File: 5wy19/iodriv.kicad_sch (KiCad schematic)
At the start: 5 parts, among them IC10 MC33385, IC3 74HCT574, IC4 HIP0045, IC6 MC33385, IC8 MC33385

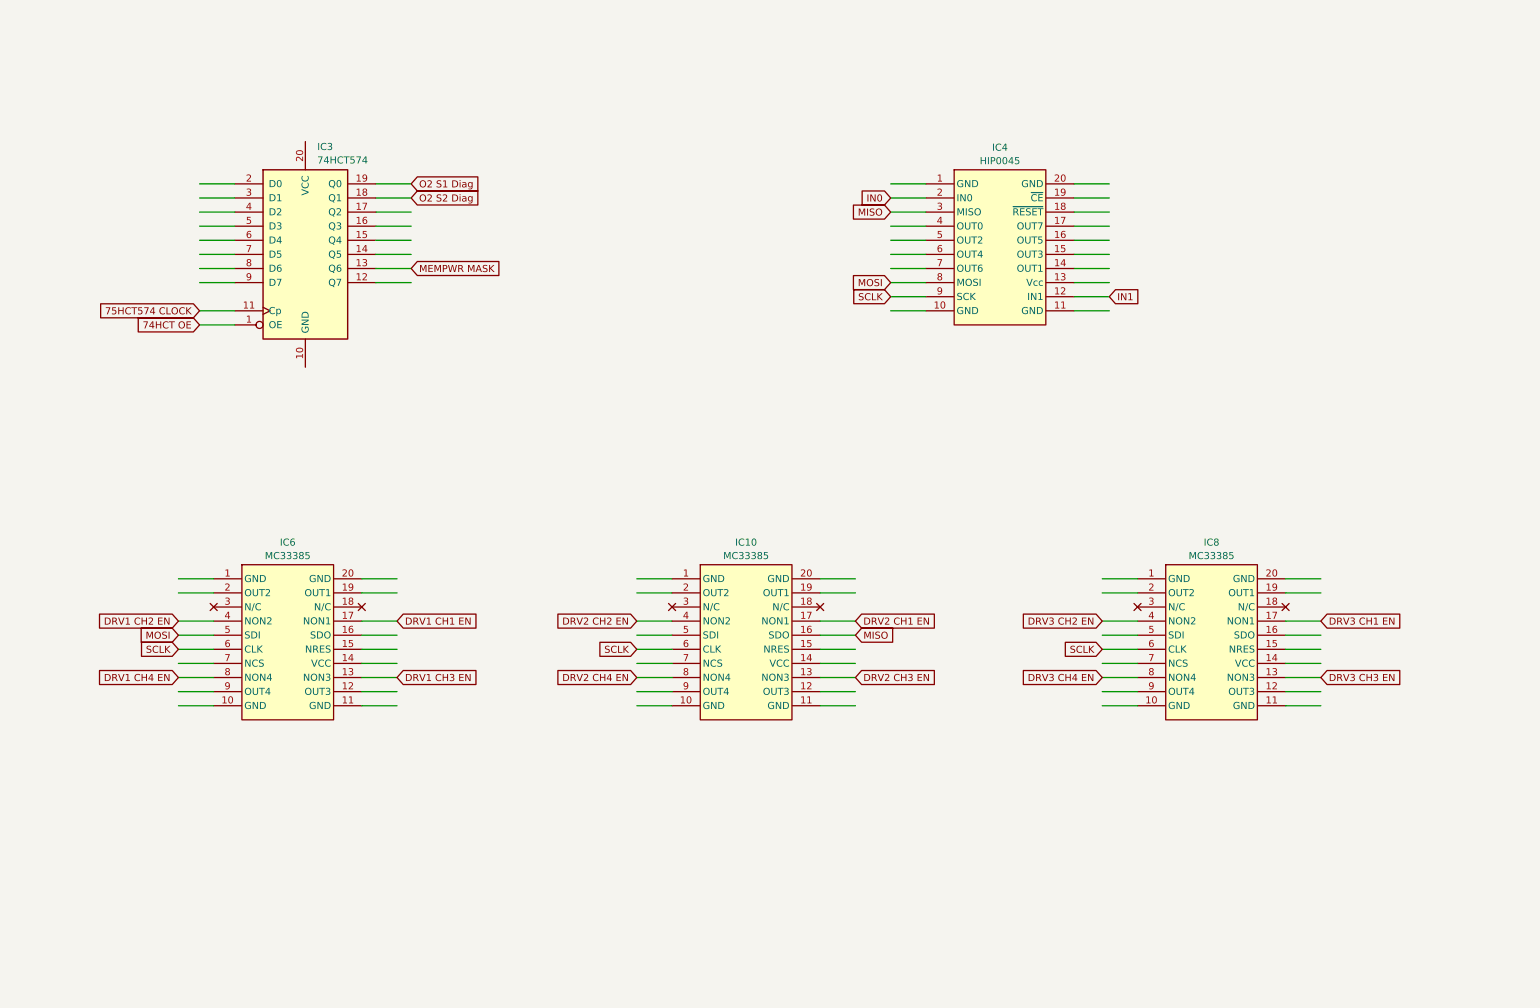
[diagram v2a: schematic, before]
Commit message: Finished most of the subsystems
-- MCU finished
-- Flash finished
-- Power Supply finished
-- I/O Drivers finished
-- CANBUS finished
-- Knock Control finished
-- Connector finished
-- Ignition Driver finished
-- Sensor Logic mostly finished
-- Logic ICs need some work
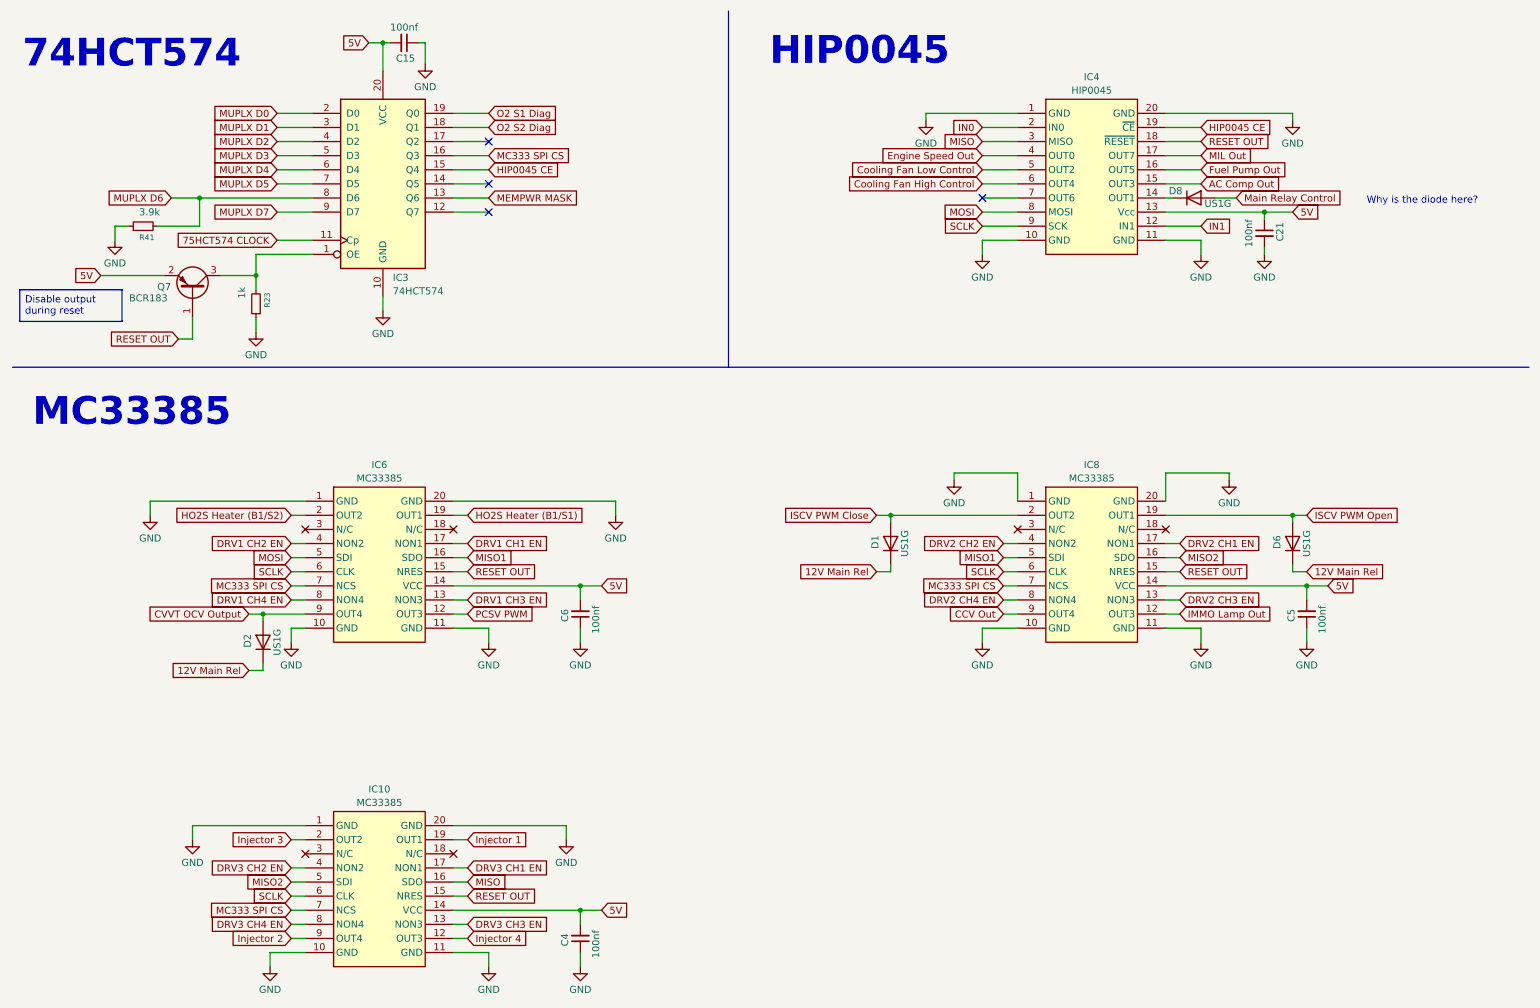
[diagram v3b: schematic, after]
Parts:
- added C15, C21, C4, C5, C6: 100nf, symbol Device:C_Small
- added D1, D2, D6, D8: US1G, Diode_SMD:D_SMA, symbol Diode:US1G
- added Q7: BCR183, Package_TO_SOT_SMD:SOT-23, symbol Transistor_BJT:BC807
- added R23: 1k, symbol Device:R_Small
- added R41: 3.9k, symbol Device:R_Small
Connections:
- net DRV2 CH1 EN: now also IC8.17 (NON1); no longer IC10.17 (NON1)
- net DRV2 CH2 EN: now also IC8.4 (NON2); no longer IC10.4 (NON2)
- net DRV2 CH3 EN: now also IC8.13 (NON3); no longer IC10.13 (NON3)
- net DRV2 CH4 EN: now also IC8.8 (NON4); no longer IC10.8 (NON4)
- net DRV3 CH1 EN: now also IC10.17 (NON1); no longer IC8.17 (NON1)
- net DRV3 CH2 EN: now also IC10.4 (NON2); no longer IC8.4 (NON2)
- net DRV3 CH3 EN: now also IC10.13 (NON3); no longer IC8.13 (NON3)
- net DRV3 CH4 EN: now also IC10.8 (NON4); no longer IC8.8 (NON4)
- net GND: now reaches IC6.1 (GND)
- net GND: now also IC10.1 (GND), IC10.10 (GND), IC10.11 (GND), IC10.20 (GND), IC3.10 (GND), IC4.1 (GND), IC4.10 (GND), IC4.11 (GND), IC4.20 (GND), IC6.10 (GND), IC6.11 (GND), IC6.20 (GND), IC8.1 (GND), IC8.10 (GND), IC8.11 (GND), IC8.20 (GND), C15.1, C21.2, C4.1, C5.1, C6.1, R23.1, R41.1
- net PCSV PWM: now reaches IC6.12 (OUT3)
- net 5V: now reaches IC6.14 (VCC)
- net 5V: now also IC10.14 (VCC), IC3.20 (VCC), IC4.13 (Vcc), IC8.14 (VCC), C15.2, C21.1, C4.2, C5.2, C6.2, Q7.2 (E)
- net RESET OUT: now reaches IC6.15 (NRES)
- net RESET OUT: now also IC10.15 (NRES), IC4.18 (~{RESET}), IC8.15 (NRES), Q7.1 (B)
- net MISO1: now reaches IC6.16 (SDO)
- net MISO1: now also IC8.5 (SDI)
- net HO2S Heater (B1/S1): now reaches IC6.19 (OUT1)
- net HO2S Heater (B1/S2): now reaches IC6.2 (OUT2)
- net MC333 SPI CS: now reaches IC6.7 (NCS)
- net MC333 SPI CS: now also IC10.7 (NCS), IC3.16 (Q3), IC8.7 (NCS)
- net CVVT OCV Output: now reaches IC6.9 (OUT4)
- net CVVT OCV Output: now also D2.2 (A)
- net at IC4.14 (OUT1): now also D8.1 (K)
- net AC Comp Out: now reaches IC4.15 (OUT3)
- net Fuel Pump Out: now reaches IC4.16 (OUT5)
- net MIL Out: now reaches IC4.17 (OUT7)
- net HIP0045 CE: now reaches IC4.19 (~{CE})
- net HIP0045 CE: now also IC3.15 (Q4)
- net Engine Speed Out: now reaches IC4.4 (OUT0)
- net Cooling Fan Low Control: now reaches IC4.5 (OUT2)
- net Cooling Fan High Control: now reaches IC4.6 (OUT4)
- net MUPLX D0: now reaches IC3.2 (D0)
- net MUPLX D1: now reaches IC3.3 (D1)
- net MUPLX D2: now reaches IC3.4 (D2)
- net MUPLX D3: now reaches IC3.5 (D3)
- net MUPLX D4: now reaches IC3.6 (D4)
- net MUPLX D5: now reaches IC3.7 (D5)
- net MUPLX D6: now reaches IC3.8 (D6)
- net MUPLX D6: now also R41.2
- net MUPLX D7: now reaches IC3.9 (D7)
- net IMMO Lamp Out: now reaches IC8.12 (OUT3)
- net MISO2: now reaches IC8.16 (SDO)
- net MISO2: now also IC10.5 (SDI)
- net ISCV PWM Open: now reaches IC8.19 (OUT1)
- net ISCV PWM Open: now also D6.2 (A)
- net ISCV PWM Close: now reaches IC8.2 (OUT2)
- net ISCV PWM Close: now also D1.2 (A)
- net CCV Out: now reaches IC8.9 (OUT4)
- net Injector 4: now reaches IC10.12 (OUT3)
- net Injector 1: now reaches IC10.19 (OUT1)
- net Injector 3: now reaches IC10.2 (OUT2)
- net Injector 2: now reaches IC10.9 (OUT4)
- net 74HCT OE: no longer names the net of IC3.1 (OE)
- net 74HCT OE: now also Q7.3 (C), R23.2
- new net 12V Main Rel: D1.1 (K), D2.1 (K), D6.1 (K)
- new net Main Relay Control: D8.2 (A)
- no-connect marks 0 -> 4
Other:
- note added: "74HCT574"
- note added: "HIP0045"
- note added: "MC33385"
- note added: "Why is the diode here?"
- title: (none) -> SMIK43 5WY19 Rev. Eng
- moved on the sheet: IC10, IC3, IC4, IC6, IC8

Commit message: Final schematic (except maybe some oversights)
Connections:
- net 5V: now also C4.1; no longer C4.2
- net GND: now also C4.2, R23.2; no longer C4.1, R23.1
- net at IC3.1 (OE), Q7.3 (C): now also R23.1; no longer R23.2
- net MUPLX D0 renamed MLTPLX D0
- net MUPLX D1 renamed MLTPLX D1
- net MUPLX D2 renamed MLTPLX D2
- net MUPLX D3 renamed MLTPLX D3
- net MUPLX D4 renamed MLTPLX D4
- net MUPLX D5 renamed MLTPLX D5
- net MUPLX D6 renamed MLTPLX D6
- net MUPLX D7 renamed MLTPLX D7
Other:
- moved on the sheet: C4, R23
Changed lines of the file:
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@@
 		)
 	)
-	(global_label "MUPLX D0"
-		(shape input)
-		(at 59.69 30.48 180)
-		(fields_autoplaced yes)
-		(effects
-			(font
-				(size 1.27 1.27)
-			)
-			(justify right)
-		)
-		(property "Intersheetrefs" "${INTERSHEET_REFS}"
-			(at 46.9682 30.48 0)
-			(effects
-				(font
-					(size 1.27 1.27)
-				)
-				(justify right)
-				(hide yes)
-			)
-		)
-	)
 	(global_label "Injector 4"
 		(shape input)
@@
 		)
 	)
-	(global_label "MUPLX D4"
-		(shape input)
-		(at 59.69 40.64 180)
-		(fields_autoplaced yes)
-		(effects
-			(font
-				(size 1.27 1.27)
-			)
-			(justify right)
-		)
-		(property "Intersheetrefs" "${INTERSHEET_REFS}"
-			(at 46.9682 40.64 0)
-			(effects
-				(font
-					(size 1.27 1.27)
-				)
-				(justify right)
-				(hide yes)
-			)
-		)
-	)
 	(global_label "DRV3 CH1 EN"
 		(shape input)
@@
 		)
 	)
-	(global_label "MUPLX D6"
+	(global_label "5V"
 		(shape input)
-		(at 40.64 45.72 180)
+		(at 27.94 59.69 180)
 		(fields_autoplaced yes)
 		(effects
@@
 		)
 		(property "Intersheetrefs" "${INTERSHEET_REFS}"
-			(at 27.9182 45.72 0)
+			(at 22.6567 59.69 0)
 			(effects
 				(font
@@
 		)
 	)
-	(global_label "5V"
+	(global_label "MLTPLX D5"
 		(shape input)
-		(at 27.94 59.69 180)
+		(at 59.69 43.18 180)
 		(fields_autoplaced yes)
 		(effects
@@
 		)
 		(property "Intersheetrefs" "${INTERSHEET_REFS}"
-			(at 22.6567 59.69 0)
+			(at 46.303 43.18 0)
 			(effects
 				(font
@@
 		)
 	)
+	(global_label "MLTPLX D7"
+		(shape input)
+		(at 59.69 48.26 180)
+		(fields_autoplaced yes)
+		(effects
+			(font
+				(size 1.27 1.27)
+			)
+			(justify right)
+		)
+		(property "Intersheetrefs" "${INTERSHEET_REFS}"
+			(at 46.303 48.26 0)
+			(effects
+				(font
+					(size 1.27 1.27)
+				)
+				(justify right)
+				(hide yes)
+			)
+		)
+	)
+	(global_label "MLTPLX D6"
+		(shape input)
+		(at 40.64 45.72 180)
+		(fields_autoplaced yes)
+		(effects
+			(font
+				(size 1.27 1.27)
+			)
+			(justify right)
+		)
+		(property "Intersheetrefs" "${INTERSHEET_REFS}"
+			(at 27.253 45.72 0)
+			(effects
+				(font
+					(size 1.27 1.27)
+				)
+				(justify right)
+				(hide yes)
+			)
+		)
+	)
 	(global_label "12V Main Rel"
 		(shape input)
@@
 		)
 	)
-	(global_label "MUPLX D1"
-		(shape input)
-		(at 59.69 33.02 180)
-		(fields_autoplaced yes)
-		(effects
-			(font
-				(size 1.27 1.27)
-			)
-			(justify right)
-		)
-		(property "Intersheetrefs" "${INTERSHEET_REFS}"
-			(at 46.9682 33.02 0)
-			(effects
-				(font
-					(size 1.27 1.27)
-				)
-				(justify right)
-				(hide yes)
-			)
-		)
-	)
 	(global_label "5V"
 		(shape input)
@@
 		)
 	)
-	(global_label "MUPLX D3"
+	(global_label "MLTPLX D2"
 		(shape input)
-		(at 59.69 38.1 180)
+		(at 59.69 35.56 180)
 		(fields_autoplaced yes)
 		(effects
@@
 		)
 		(property "Intersheetrefs" "${INTERSHEET_REFS}"
-			(at 46.9682 38.1 0)
+			(at 46.303 35.56 0)
 			(effects
 				(font
@@
 		)
 	)
+	(global_label "MLTPLX D3"
+		(shape input)
+		(at 59.69 38.1 180)
+		(fields_autoplaced yes)
+		(effects
+			(font
+				(size 1.27 1.27)
+			)
+			(justify right)
+		)
+		(property "Intersheetrefs" "${INTERSHEET_REFS}"
+			(at 46.303 38.1 0)
+			(effects
+				(font
+					(size 1.27 1.27)
+				)
+				(justify right)
+				(hide yes)
+			)
+		)
+	)
 	(global_label "MISO2"
 		(shape input)
@@
 		)
 	)
-	(global_label "DRV2 CH1 EN"
+	(global_label "MLTPLX D1"
 		(shape input)
-		(at 222.25 107.95 0)
+		(at 59.69 33.02 180)
 		(fields_autoplaced yes)
 		(effects
@@
 				(size 1.27 1.27)
 			)
-			(justify left)
+			(justify right)
 		)
 		(property "Intersheetrefs" "${INTERSHEET_REFS}"
-			(at 238.298 107.95 0)
+			(at 46.303 33.02 0)
 			(effects
 				(font
 					(size 1.27 1.27)
 				)
-				(justify left)
+				(justify right)
 				(hide yes)
 			)
 		)
 	)
-	(global_label "DRV2 CH3 EN"
+	(global_label "DRV2 CH1 EN"
 		(shape input)
-		(at 222.25 118.11 0)
+		(at 222.25 107.95 0)
 		(fields_autoplaced yes)
 		(effects
@@
 		)
 		(property "Intersheetrefs" "${INTERSHEET_REFS}"
-			(at 238.298 118.11 0)
+			(at 238.298 107.95 0)
 			(effects
 				(font
@@
 		)
 	)
-	(global_label "MUPLX D7"
+	(global_label "DRV2 CH3 EN"
 		(shape input)
-		(at 59.69 48.26 180)
+		(at 222.25 118.11 0)
 		(fields_autoplaced yes)
 		(effects
@@
 				(size 1.27 1.27)
 			)
-			(justify right)
+			(justify left)
 		)
 		(property "Intersheetrefs" "${INTERSHEET_REFS}"
-			(at 46.9682 48.26 0)
+			(at 238.298 118.11 0)
 			(effects
 				(font
 					(size 1.27 1.27)
 				)
-				(justify right)
+				(justify left)
 				(hide yes)
 			)
@@
 		)
 	)
-	(global_label "MUPLX D5"
+	(global_label "MIL Out"
 		(shape input)
-		(at 59.69 43.18 180)
+		(at 226.06 38.1 0)
 		(fields_autoplaced yes)
 		(effects
@@
 				(size 1.27 1.27)
 			)
-			(justify right)
+			(justify left)
 		)
 		(property "Intersheetrefs" "${INTERSHEET_REFS}"
-			(at 46.9682 43.18 0)
+			(at 236.3023 38.1 0)
 			(effects
 				(font
 					(size 1.27 1.27)
 				)
-				(justify right)
+				(justify left)
 				(hide yes)
 			)
 		)
 	)
-	(global_label "MIL Out"
+	(global_label "SCLK"
 		(shape input)
-		(at 226.06 38.1 0)
+		(at 62.23 113.03 180)
 		(fields_autoplaced yes)
 		(effects
@@
 				(size 1.27 1.27)
 			)
-			(justify left)
+			(justify right)
 		)
 		(property "Intersheetrefs" "${INTERSHEET_REFS}"
-			(at 236.3023 38.1 0)
+			(at 54.4672 113.03 0)
 			(effects
 				(font
 					(size 1.27 1.27)
 				)
-				(justify left)
+				(justify right)
 				(hide yes)
 			)
 		)
 	)
-	(global_label "SCLK"
+	(global_label "Injector 3"
 		(shape input)
-		(at 62.23 113.03 180)
+		(at 62.23 161.29 180)
 		(fields_autoplaced yes)
 		(effects
@@
 		)
 		(property "Intersheetrefs" "${INTERSHEET_REFS}"
-			(at 54.4672 113.03 0)
+			(at 49.871 161.29 0)
 			(effects
 				(font
@@
 		)
 	)
-	(global_label "MUPLX D2"
+	(global_label "MLTPLX D0"
 		(shape input)
-		(at 59.69 35.56 180)
+		(at 59.69 30.48 180)
 		(fields_autoplaced yes)
 		(effects
@@
 		)
 		(property "Intersheetrefs" "${INTERSHEET_REFS}"
-			(at 46.9682 35.56 0)
+			(at 46.303 30.48 0)
 			(effects
 				(font
@@
 		)
 	)
-	(global_label "Injector 3"
+	(global_label "MISO2"
 		(shape input)
-		(at 62.23 161.29 180)
+		(at 222.25 110.49 0)
 		(fields_autoplaced yes)
 		(effects
@@
 				(size 1.27 1.27)
 			)
-			(justify right)
+			(justify left)
 		)
 		(property "Intersheetrefs" "${INTERSHEET_REFS}"
-			(at 49.871 161.29 0)
+			(at 231.0409 110.49 0)
 			(effects
 				(font
 					(size 1.27 1.27)
 				)
-				(justify right)
+				(justify left)
 				(hide yes)
 			)
 		)
 	)
-	(global_label "MISO2"
+	(global_label "MLTPLX D4"
 		(shape input)
-		(at 222.25 110.49 0)
+		(at 59.69 40.64 180)
 		(fields_autoplaced yes)
 		(effects
@@
 				(size 1.27 1.27)
 			)
-			(justify left)
+			(justify right)
 		)
 		(property "Intersheetrefs" "${INTERSHEET_REFS}"
-			(at 231.0409 110.49 0)
+			(at 46.303 40.64 0)
 			(effects
 				(font
 					(size 1.27 1.27)
 				)
-				(justify left)
+				(justify right)
 				(hide yes)
 			)
@@
 	(symbol
 		(lib_id "Device:C_Small")
-		(at 114.3 179.07 180)
+		(at 114.3 179.07 0)
 		(unit 1)
 		(exclude_from_sim no)
@@
 		(dnp no)
 		(property "Reference" "C4"
-			(at 111.506 179.324 90)
+			(at 117.094 178.816 90)
 			(effects
 				(font
@@
 		)
 		(property "Value" "100nf"
-			(at 117.094 180.086 90)
+			(at 111.506 178.054 90)
 			(effects
 				(font
@@
 	(symbol
 		(lib_id "Device:R_Small")
-		(at 55.88 64.77 180)
+		(at 55.88 64.77 0)
 		(unit 1)
 		(exclude_from_sim no)
@@
 		(dnp no)
 		(property "Reference" "R23"
-			(at 57.912 62.738 90)
+			(at 53.848 66.802 90)
 			(effects
 				(font
@@
 		)
 		(property "Value" "1k"
-			(at 53.34 61.722 90)
+			(at 58.42 67.818 90)
 			(effects
 				(font
